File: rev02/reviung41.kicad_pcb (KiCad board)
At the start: 2 copper layers, 85 parts, among them SW10 SW_PUSH, SW11 SW_PUSH, SW12 SW_PUSH, SW14 SW_PUSH, SW15 SW_PUSH, SW16 SW_PUSH, SW17 SW_PUSH, SW18 SW_PUSH, SW19 SW_PUSH, SW2 SW_PUSH, SW20 SW_PUSH, SW21 SW_PUSH, SW22 SW_PUSH, SW23 SW_PUSH, SW25 SW_PUSH, SW26 SW_PUSH, SW27 SW_PUSH, SW28 SW_PUSH, SW29 SW_PUSH, SW3 SW_PUSH, SW31 SW_PUSH, SW32 SW_PUSH, SW33 SW_PUSH, SW34 SW_PUSH, SW35 SW_PUSH, SW37 SW_PUSH, SW38 SW_PUSH, SW39 SW_PUSH, SW4 SW_PUSH, SW40 SW_PUSH, SW41 SW_PUSH, SW42 SW_PUSH, SW5 SW_PUSH, SW6 SW_PUSH, SW8 SW_PUSH, SW9 SW_PUSH, U1 ProMicro

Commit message: Rev02: Fixed a couple of switch positions and placed all the resistors
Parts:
- moved D29 349.7 mm to (275.3, 71.7), turned to 105 degrees
- moved D28 343.9 mm to (254.2, 66.8), turned to 105 degrees
- moved D23 336.6 mm to (270.3, 53.3), turned to 105 degrees
- moved D27 329.4 mm to (234.5, 66.8), turned to 105 degrees
- moved D22 326.0 mm to (249.3, 48.4), turned to 105 degrees
- moved D35 324.2 mm to (280.2, 90.1), turned to 105 degrees
- moved D21 311.2 mm to (229.6, 48.4), turned to 105 degrees
- moved D34 310.0 mm to (259.2, 85.2), turned to 105 degrees
- moved D33 304.0 mm to (239.5, 85.2), turned to 105 degrees
- moved D20 297.5 mm to (212.5, 58.3), turned to 105 degrees
- moved D32 282.5 mm to (222.4, 95.1), turned to 105 degrees
- moved D19 279.1 mm to (194.8, 65.6), turned to 105 degrees
- moved D3 278.2 mm to (90.7, 52.7), turned to 75 degrees
- moved D26 274.8 mm to (217.4, 76.7), turned to 105 degrees
- moved D41 273.3 mm to (230.6, 125.7), turned to 105 degrees
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
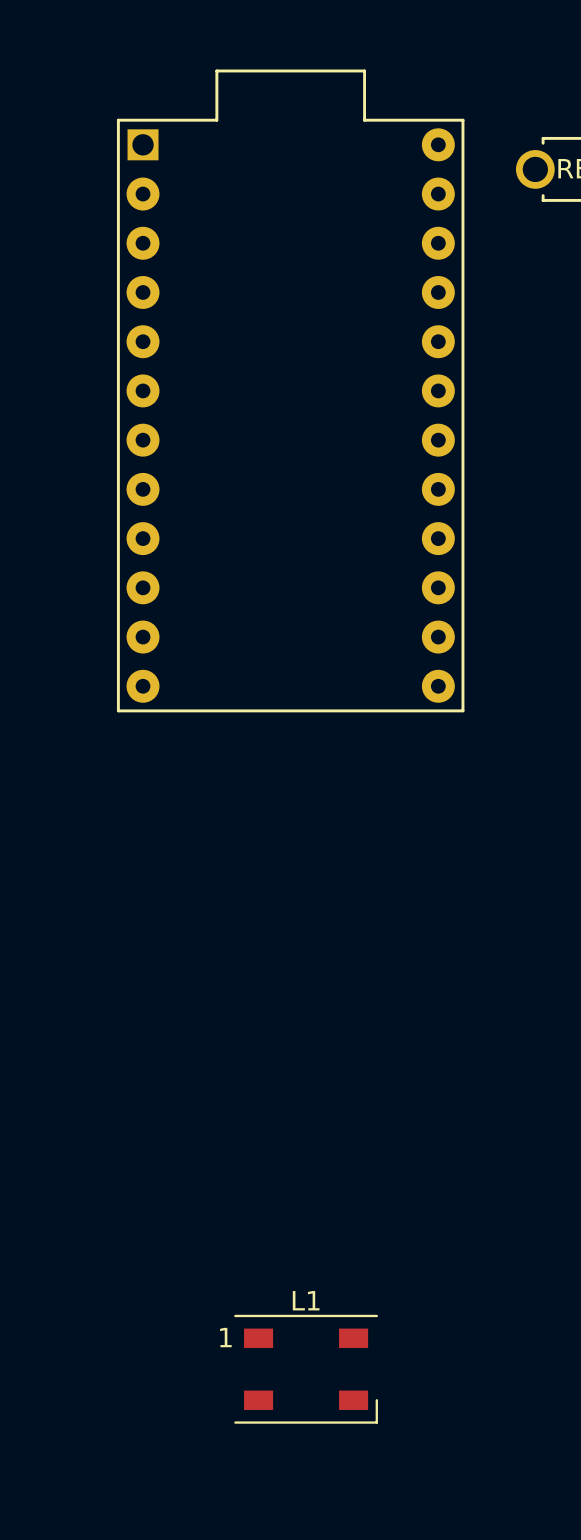
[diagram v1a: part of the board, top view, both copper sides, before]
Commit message: centered some components more precisely
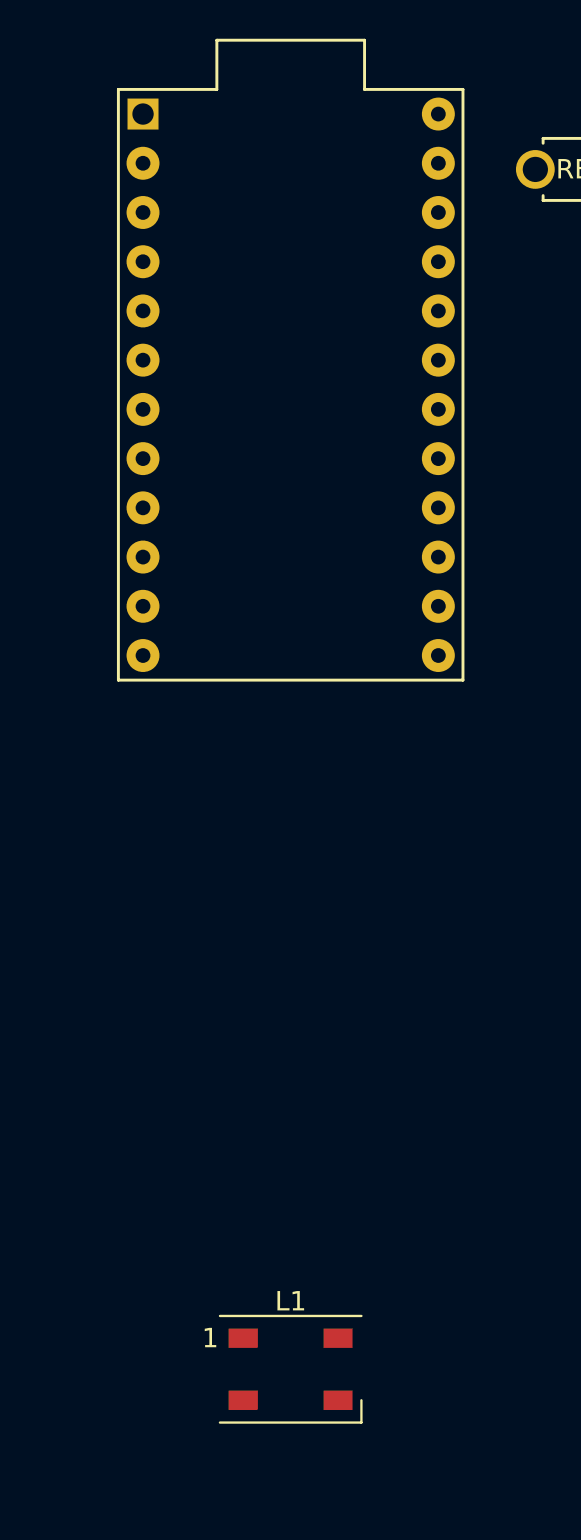
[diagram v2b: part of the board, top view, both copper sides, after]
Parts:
- moved U1 1.59 mm to (161.9, 52.4)
- moved L1 0.79 mm to (161.9, 103.2)
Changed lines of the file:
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@@
   )
   (module _reviung-kbd:ProMicro (layer F.Cu)
-    (at 161.925 53.975 270)
+    (at 161.925 52.3875 270)
     (descr "Pro Micro footprint")
     (tags "promicro ProMicro")
@@
   )
   (module _reviung-kbd:LED_WS2812B_PLCC4_5.0x5.0mm_P3.2mm (layer F.Cu)
-    (at 162.71875 103.1875)
+    (at 161.925 103.1875)
     (descr https://cdn-shop.adafruit.com/datasheets/WS2812B.pdf)
     (tags "LED RGB NeoPixel")

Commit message: added edge outline
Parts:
- moved D15 16.2 mm to (69.4, 78.0)
- moved D16 16.2 mm to (89.2, 78.1)
- moved D19 16.2 mm to (183.3, 54.2)
- moved D25 16.2 mm to (188.3, 72.6)
- moved D26 16.2 mm to (206.0, 65.2)
- moved D29 16.2 mm to (263.8, 60.3)
- moved D31 16.2 mm to (193.2, 91.0)
- moved D32 16.2 mm to (210.9, 83.6)
- moved D35 16.2 mm to (268.8, 78.7)
- moved D39 16.2 mm to (136.0, 139.9)
- moved D40 16.2 mm to (198.2, 120.9)
- moved L1 16.2 mm to (150.5, 91.8)
- moved L5 16.2 mm to (69.5, 107.6)
- moved L6 16.2 mm to (125.1, 122.7)
- moved L8 16.2 mm to (233.0, 108.4)
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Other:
- board outline added: 250.2 x 127 mm

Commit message: First round of working on rounting, wip
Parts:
- U1: moved to B.Cu
- moved RESET1 34.6 mm to (131.8, 29.8)
- moved D10 19.7 mm to (94.1, 59.7)
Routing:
- net GND: track 0.00 -> 607.1 mm, vias 0 -> 1
- net col1: track 0.00 -> 563.0 mm, vias 0 -> 11
- net col2: track 0.00 -> 528.7 mm, vias 0 -> 12
- net col3: track 0.00 -> 476.0 mm, vias 0 -> 6
- net col0: track 0.00 -> 162.7 mm, vias 0 -> 2
- net Net-(D17-Pad2): track 0.00 -> 4.43 mm
- net Net-(D14-Pad2): track 0.00 -> 4.43 mm
- net Net-(D37-Pad2): track 0.00 -> 4.43 mm
- net Net-(D16-Pad2): track 0.00 -> 4.43 mm
- net Net-(D15-Pad2): track 0.00 -> 4.43 mm
- net Net-(D12-Pad2): track 0.00 -> 4.43 mm
- net Net-(D8-Pad2): track 0.00 -> 4.43 mm
- net Net-(D6-Pad2): track 0.00 -> 4.43 mm
- net Net-(D4-Pad2): track 0.00 -> 4.43 mm
- net Net-(D11-Pad2): track 0.00 -> 4.43 mm
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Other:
- net class Default: via_dia 0.6 -> 31.49606; via_drill 0.3 -> 0.4
- net class Power added: clearance 0.2, trace_width 0.381, via_dia 31.49606, via_drill 0.4

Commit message: completed all routing, still have unconnected stuff in DRC, need to fix
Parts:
- moved L9 1.20 mm to (252.5, 70.1)
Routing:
- net VCC: track 0.00 -> 631.6 mm, vias 0 -> 9
- net col4: track 0.00 -> 499.8 mm, vias 0 -> 10
- net row6: track 0.00 -> 238.0 mm, vias 0 -> 10
- net col5: track 0.00 -> 187.4 mm, vias 0 -> 2
- net row5: track 0.00 -> 176.3 mm, vias 0 -> 11
- net row4: track 0.00 -> 171.1 mm, vias 0 -> 11
- net row3: track 0.00 -> 167.5 mm, vias 0 -> 11
- net row2: track 0.00 -> 152.2 mm, vias 0 -> 8
- net row1: track 0.00 -> 139.2 mm, vias 0 -> 10
- net row0: track 0.00 -> 123.6 mm, vias 0 -> 8
- net GND: track 607.1 -> 695.6 mm, vias 1 -> 5
- net Net-(L4-Pad2): track 0.00 -> 78.9 mm, vias 0 -> 2
- net Net-(L1-Pad2): track 0.00 -> 76.0 mm, vias 0 -> 1
- net Net-(L6-Pad2): track 0.00 -> 74.4 mm, vias 0 -> 2
- net Net-(L7-Pad2): track 0.00 -> 73.2 mm, vias 0 -> 2
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
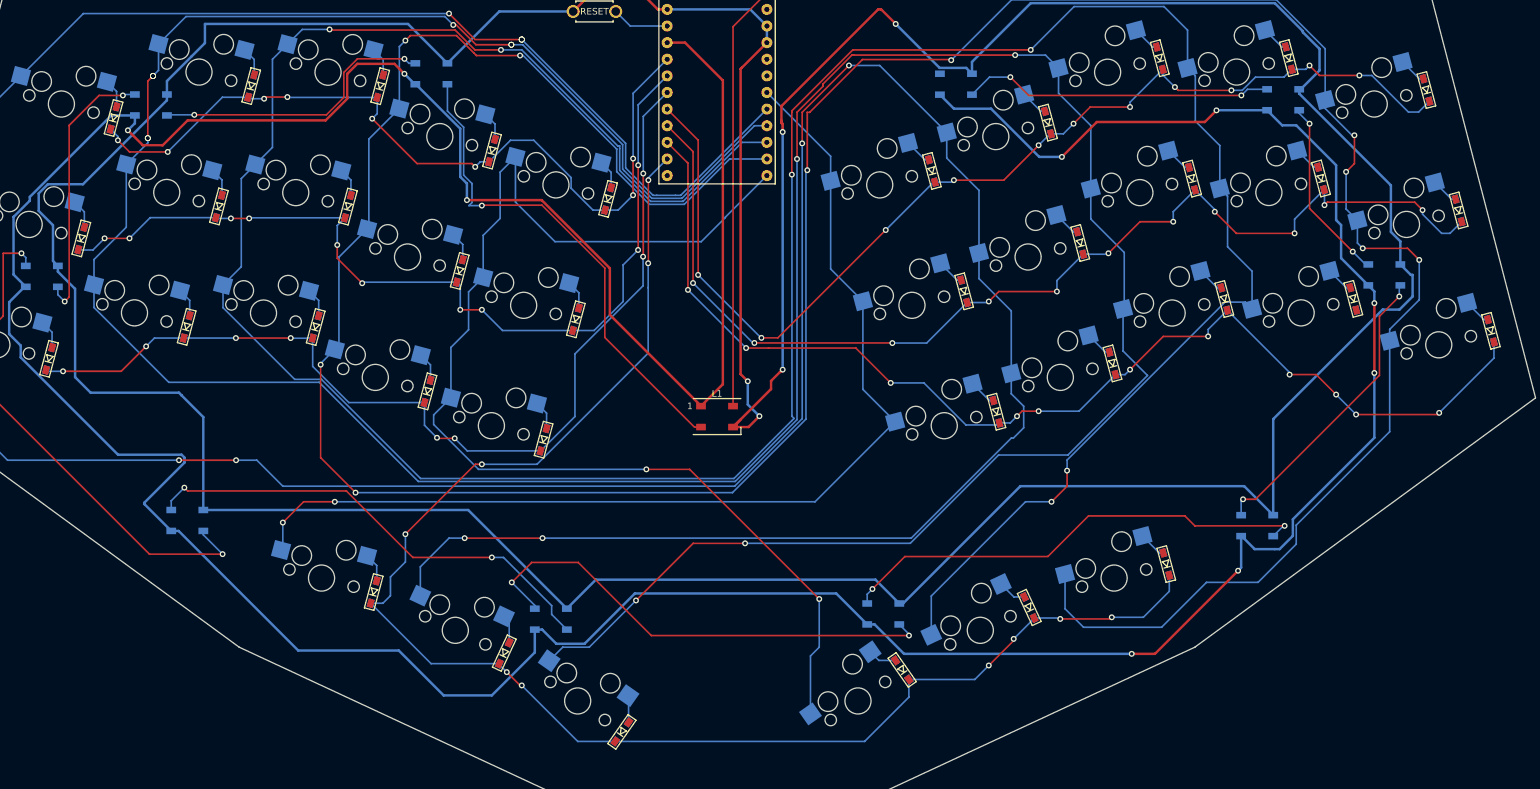
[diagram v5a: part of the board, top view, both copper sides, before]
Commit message: Some major changes, replaced diodes with SOD123, fixed some routing, updated footprints to use different libraries
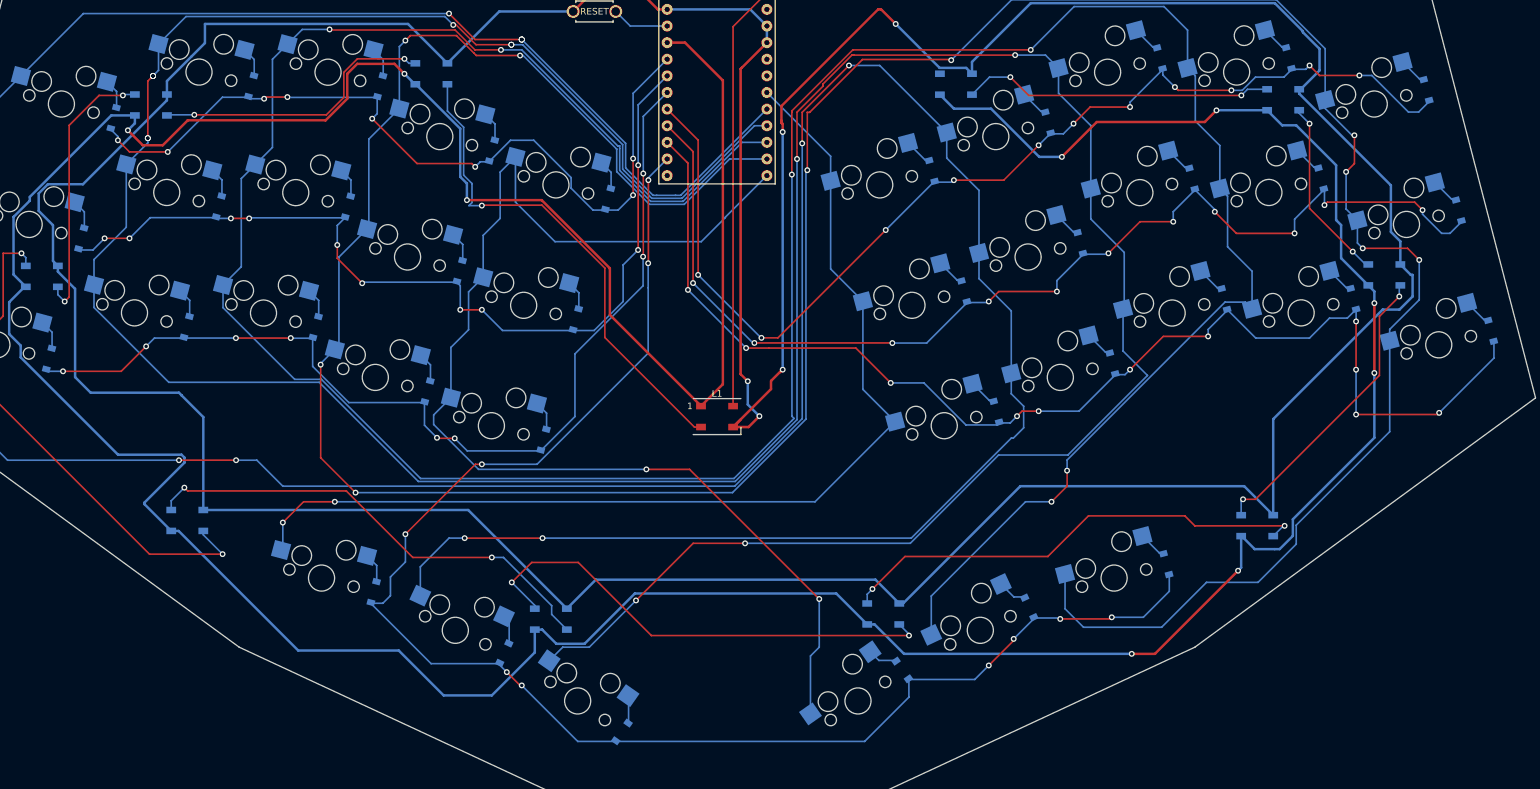
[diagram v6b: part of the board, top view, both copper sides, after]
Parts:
- D10, D11, D12, D14, D15, D16, D17, D18, D19, D2, D20, D21, D22, D23, D25, D26, D27, D28, D29, D3, D31, D32, D33, D34, D35, D37, D38, D39, D4, D40, D41, D42, D5, D6, D8, D9: footprint _reviung-kbd:D3_SMD_1side -> Diode_SMD:D_SOD-123; moved to B.Cu
- L1, L10, L11, L2, L3, L4, L5, L6, L7, L8, L9: footprint _reviung-kbd:LED_WS2812B_PLCC4_5.0x5.0mm_P3.2mm -> LED_SMD:LED_WS2812B_PLCC4_5.0x5.0mm_P3.2mm
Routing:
- net row5: track 176.3 -> 189.2 mm

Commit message: euclid36 rev, sent to production...
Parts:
- added L12: WS2812B, LED_SMD:LED_WS2812B_PLCC4_5.0x5.0mm_P3.2mm, B.Cu at (237.0, 43.3)
- added L13: WS2812B, LED_SMD:LED_WS2812B_PLCC4_5.0x5.0mm_P3.2mm, B.Cu at (187.0, 41.1)
- L2, L3: moved to F.Cu
- moved L3 113.7 mm to (165.1, 96.0)
- moved L8 108.9 mm to (125.1, 122.7)
- moved L7 107.3 mm to (69.6, 107.7)
- moved L6 93.8 mm to (47.3, 70.2)
- moved L9 92.5 mm to (175.9, 122.0)
- moved L11 71.5 mm to (252.3, 70.0)
- moved L4 67.1 mm to (106.9, 39.3)
- moved L10 65.2 mm to (233.0, 108.4)
- moved L5 63.8 mm to (64.0, 44.1)
- moved L2 63.6 mm to (135.7, 96.0)
- moved L1 19.5 mm to (150.6, 72.2)
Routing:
- net VCC: track 631.6 -> 695.5 mm, vias 9 -> 15
- net GND: track 695.6 -> 642.0 mm, vias 5 -> 0
- net Net-(L3-Pad2): track 41.9 -> 93.2 mm, vias 2 -> 5
- net Net-(L1-Pad2): track 76.0 -> 24.7 mm, vias 1 -> 0
- net Net-(L12-Pad2): track 0.00 -> 47.8 mm, vias 0 -> 2
- net Net-(L10-Pad4): track 28.2 -> 73.2 mm
- net Net-(L4-Pad2): track 78.9 -> 44.1 mm
- net Net-(L5-Pad2): track 72.5 -> 41.9 mm
- net Net-(L11-Pad2): track 0.00 -> 28.2 mm, vias 0 -> 2
- net Net-(L8-Pad2): track 46.3 -> 74.4 mm
- net LED: track 65.3 -> 45.8 mm
- net Net-(L6-Pad2): track 74.4 -> 78.9 mm
- net row5: track 189.2 -> 193.6 mm, vias 11 -> 12
- net row4: track 171.1 -> 174.3 mm, vias 11 -> 12
- net Net-(L2-Pad2): track 44.1 -> 46.5 mm, vias 2 -> 0
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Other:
- board size 250.2 x 127 mm -> 248.2 x 127 mm
